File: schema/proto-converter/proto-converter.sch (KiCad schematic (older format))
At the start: 35 parts, among them P1 CONN_8, Q1 BC847, Q2 MOS_P, Q3 BC857, Q4 BC847, Q5 BC847, Q6 BC847, Q7 MOS_N, Q8 BC857

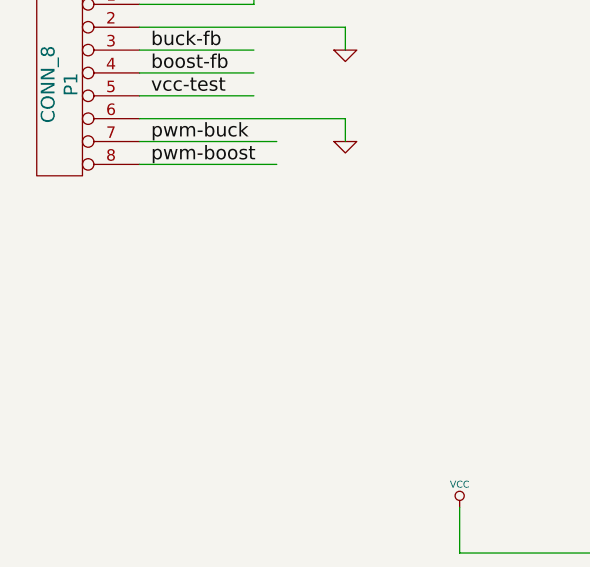
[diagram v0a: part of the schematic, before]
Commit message: Finished converter prototype.
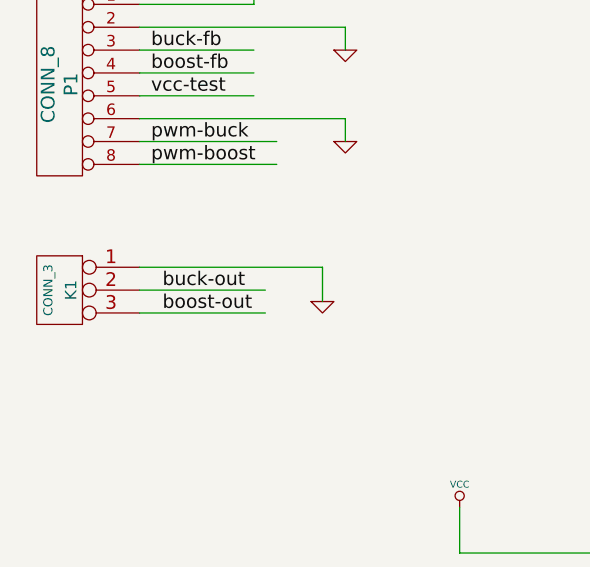
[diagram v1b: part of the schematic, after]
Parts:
- added K1: CONN_3, symbol CONN_3
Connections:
- wire segments 84 -> 88
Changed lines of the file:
@@
-EESchema Schematic File Version 2  date Sun 28 Oct 2012 12:31:00 AM MSK
+EESchema Schematic File Version 2  date Sun 28 Oct 2012 11:14:49 PM MSK
 LIBS:power
 LIBS:device
@@
 Sheet 1 1
 Title ""
-Date "27 oct 2012"
+Date "28 oct 2012"
 Rev ""
 Comp ""
@@
 $EndDescr
 Wire Wire Line
+	2100 3000 2100 2850
+Wire Wire Line
+	2100 2850 1300 2850
+Wire Wire Line
+	1300 3050 1850 3050
+Wire Wire Line
 	1900 2400 1300 2400
 Wire Wire Line
@@
 Wire Wire Line
 	1900 2300 1300 2300
+Wire Wire Line
+	1300 2950 1850 2950
+Text Label 1400 3050 0    60   ~ 0
+boost-out
+Text Label 1400 2950 0    60   ~ 0
+buck-out
+$Comp
+L GND #PWR01
+U 1 1 508D8385
+P 2100 3000
+F 0 "#PWR01" H 2100 3000 30  0001 C CNN
+F 1 "GND" H 2100 2930 30  0001 C CNN
+	1    2100 3000
+	1    0    0    -1
+$EndComp
+$Comp
+L CONN_3 K1
+U 1 1 508D836D
+P 950 2950
+F 0 "K1" V 900 2950 50  0000 C CNN
+F 1 "CONN_3" V 1000 2950 40  0000 C CNN
+	1    950  2950
+	-1   0    0    -1
+$EndComp
 Text Label 1350 2400 0    60   ~ 0
 pwm-boost
@@
 pwm-buck
 $Comp
-L GND #PWR01
+L GND #PWR02
 U 1 1 508C42EB
 P 2200 2300
-F 0 "#PWR01" H 2200 2300 30  0001 C CNN
+F 0 "#PWR02" H 2200 2300 30  0001 C CNN
 F 1 "GND" H 2200 2230 30  0001 C CNN
 	1    2200 2300
@@
 buck-fb
 $Comp
-L GND #PWR02
+L GND #PWR03
 U 1 1 508C4250
 P 2200 1900
-F 0 "#PWR02" H 2200 1900 30  0001 C CNN
+F 0 "#PWR03" H 2200 1900 30  0001 C CNN
 F 1 "GND" H 2200 1830 30  0001 C CNN
 	1    2200 1900
@@
 $EndComp
 $Comp
-L VCC #PWR03
+L VCC #PWR04
 U 1 1 508C4248
 P 1800 1600
-F 0 "#PWR03" H 1800 1700 30  0001 C CNN
+F 0 "#PWR04" H 1800 1700 30  0001 C CNN
 F 1 "VCC" H 1800 1700 30  0000 C CNN
 	1    1800 1600
@@
 $EndComp
 $Comp
-L GND #PWR04
+L GND #PWR05
 U 1 1 508C41F5
 P 1700 1300
-F 0 "#PWR04" H 1700 1300 30  0001 C CNN
+F 0 "#PWR05" H 1700 1300 30  0001 C CNN
 F 1 "GND" H 1700 1230 30  0001 C CNN
 	1    1700 1300
@@
 $EndComp
 $Comp
-L PWR_FLAG #FLG05
+L PWR_FLAG #FLG06
 U 1 1 508C41EA
 P 1700 1100
-F 0 "#FLG05" H 1700 1195 30  0001 C CNN
+F 0 "#FLG06" H 1700 1195 30  0001 C CNN
 F 1 "PWR_FLAG" H 1700 1280 30  0000 C CNN
 	1    1700 1100
@@
 $EndComp
 $Comp
-L VCC #PWR06
+L VCC #PWR07
 U 1 1 508C41E3
 P 1300 1100
-F 0 "#PWR06" H 1300 1200 30  0001 C CNN
+F 0 "#PWR07" H 1300 1200 30  0001 C CNN
 F 1 "VCC" H 1300 1200 30  0000 C CNN
 	1    1300 1100
@@
 $EndComp
 $Comp
-L PWR_FLAG #FLG07
+L PWR_FLAG #FLG08
 U 1 1 508C41D3
 P 900 1100
-F 0 "#FLG07" H 900 1195 30  0001 C CNN
+F 0 "#FLG08" H 900 1195 30  0001 C CNN
 F 1 "PWR_FLAG" H 900 1280 30  0000 C CNN
 	1    900  1100
@@
 $EndComp
 $Comp
-L VCC #PWR08
+L VCC #PWR09
 U 1 1 508C41B3
 P 10700 4500
-F 0 "#PWR08" H 10700 4600 30  0001 C CNN
+F 0 "#PWR09" H 10700 4600 30  0001 C CNN
 F 1 "VCC" H 10700 4600 30  0000 C CNN
 	1    10700 4500
@@
 vcc-test
 $Comp
-L GND #PWR09
+L GND #PWR010
 U 1 1 508C41A5
 P 10700 6800
-F 0 "#PWR09" H 10700 6800 30  0001 C CNN
+F 0 "#PWR010" H 10700 6800 30  0001 C CNN
 F 1 "GND" H 10700 6730 30  0001 C CNN
 	1    10700 6800
@@
 boost-out
 $Comp
-L GND #PWR010
+L GND #PWR011
 U 1 1 508C4173
 P 8700 6700
-F 0 "#PWR010" H 8700 6700 30  0001 C CNN
+F 0 "#PWR011" H 8700 6700 30  0001 C CNN
 F 1 "GND" H 8700 6630 30  0001 C CNN
 	1    8700 6700
@@
 boost-out
 $Comp
-L VCC #PWR011
+L VCC #PWR012
 U 1 1 508C3D30
 P 2700 5200
-F 0 "#PWR011" H 2700 5300 30  0001 C CNN
+F 0 "#PWR012" H 2700 5300 30  0001 C CNN
 F 1 "VCC" H 2700 5300 30  0000 C CNN
 	1    2700 5200
@@
 pwm-boost
 $Comp
-L VCC #PWR012
+L VCC #PWR013
 U 1 1 508C3CA1
 P 3600 5200
-F 0 "#PWR012" H 3600 5300 30  0001 C CNN
+F 0 "#PWR013" H 3600 5300 30  0001 C CNN
 F 1 "VCC" H 3600 5300 30  0000 C CNN
 	1    3600 5200
@@
 $EndComp
 $Comp
-L VCC #PWR013
+L VCC #PWR014
 U 1 1 508C3C92
 P 2700 3900
-F 0 "#PWR013" H 2700 4000 30  0001 C CNN
+F 0 "#PWR014" H 2700 4000 30  0001 C CNN
 F 1 "VCC" H 2700 4000 30  0000 C CNN
 	1    2700 3900
@@
 $EndComp
 $Comp
-L GND #PWR014
+L GND #PWR015
 U 1 1 508C3C86
 P 3100 7300
-F 0 "#PWR014" H 3100 7300 30  0001 C CNN
+F 0 "#PWR015" H 3100 7300 30  0001 C CNN
 F 1 "GND" H 3100 7230 30  0001 C CNN
 	1    3100 7300
@@
 $EndComp
 $Comp
-L GND #PWR015
+L GND #PWR016
 U 1 1 508C3C7F
 P 3600 6800
-F 0 "#PWR015" H 3600 6800 30  0001 C CNN
+F 0 "#PWR016" H 3600 6800 30  0001 C CNN
 F 1 "GND" H 3600 6730 30  0001 C CNN
 	1    3600 6800
@@
 $EndComp
 $Comp
-L GND #PWR016
+L GND #PWR017
 U 1 1 508C3BB3
 P 4800 6400
-F 0 "#PWR016" H 4800 6400 30  0001 C CNN
+F 0 "#PWR017" H 4800 6400 30  0001 C CNN
 F 1 "GND" H 4800 6330 30  0001 C CNN
 	1    4800 6400
